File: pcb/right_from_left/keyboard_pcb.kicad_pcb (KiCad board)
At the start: 2 copper layers, 138.8 x 89.9 mm, 50 parts, among them J1 TRRS, K0 KEYSW, K1 KEYSW, K10 KEYSW, K11 KEYSW, K12 KEYSW, K13 KEYSW, K14 KEYSW, K15 KEYSW, K2 KEYSW, K20 KEYSW, K21 KEYSW, K22 KEYSW, K23 KEYSW, K24 KEYSW, K25 KEYSW, K3 KEYSW, K30 KEYSW, K31 KEYSW, K32 KEYSW, K4 KEYSW, K5 KEYSW, U1 MCP23009-E/SO, U2 Pico

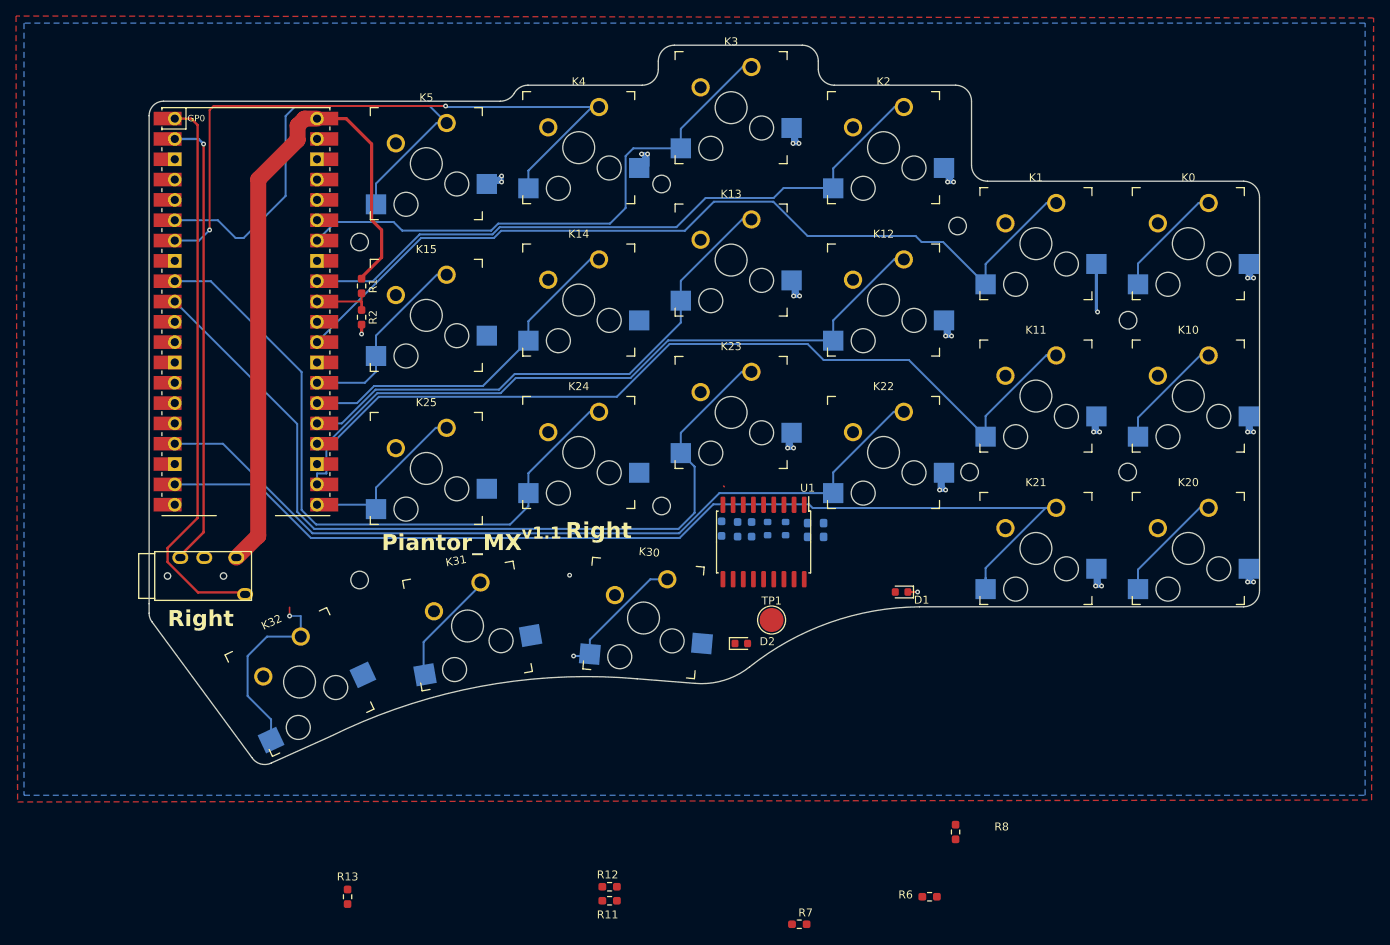
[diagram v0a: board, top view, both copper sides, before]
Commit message: Revision 1.1 -RFR- new standoff holes added and left/right pcb positions synced
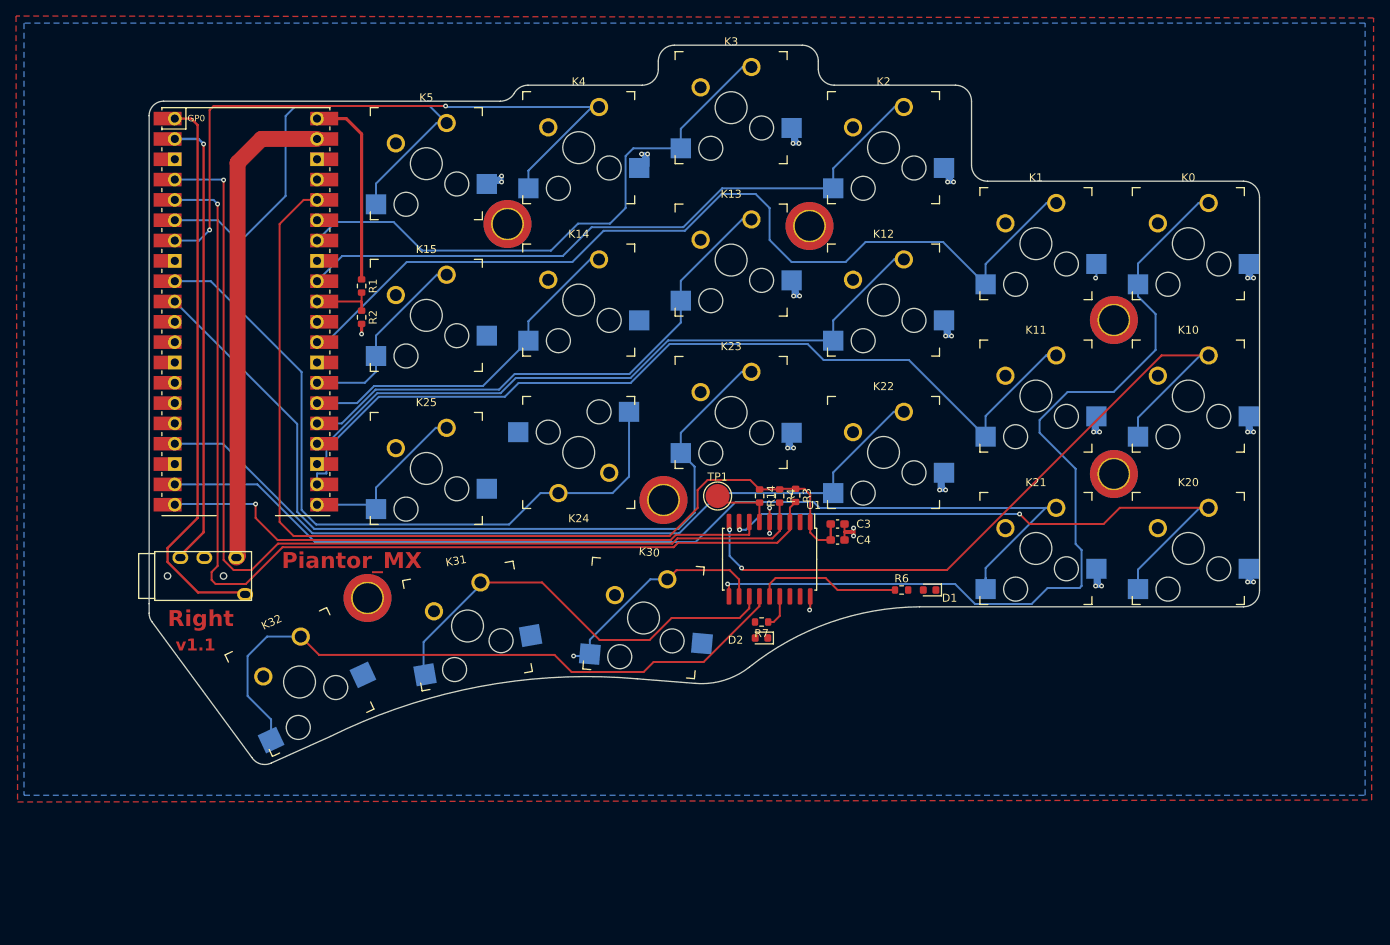
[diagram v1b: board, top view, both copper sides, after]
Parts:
- removed H7, H8: MountingHole, beekeeb_lib:MountingHole_2.2mm_M2-8mm
- removed R10, R11, R12, R13, R8, R9: 10k, Resistor_SMD:R_0603_1608Metric_Pad0.98x0.95mm_HandSolder
- C3, C4, R3, R4: moved to F.Cu
- H1, H2, H3, H4, H5, H6: footprint beekeeb_lib:MountingHole_2.2mm_M2-8mm -> misc:MountingHole_3.7mm_Pad_TopBottom
- R1, R2, R6, R7: footprint Resistor_SMD:R_0603_1608Metric_Pad0.98x0.95mm_HandSolder -> Resistor_SMD:R_0603_1608Metric
- R14: footprint Resistor_SMD:R_0603_1608Metric_Pad0.98x0.95mm_HandSolder -> Resistor_SMD:R_0603_1608Metric; moved to F.Cu
- moved R6 38.5 mm to (160.5, 111.5)
- moved R7 38.1 mm to (143.0, 115.5), turned to 180 degrees
- moved H5 22.8 mm to (187.0, 77.8)
- moved H1 19.2 mm to (149.0, 66.0)
- moved H2 18.6 mm to (111.2, 65.8)
- moved H6 18.0 mm to (187.0, 97.0)
- moved TP1 16.9 mm to (137.5, 99.8)
- moved R4 4.34 mm to (145.2, 99.8), turned to -90 degrees
- moved R3 4.33 mm to (147.2, 99.7), turned to -90 degrees
- moved R14 4.28 mm to (142.8, 99.8), turned to -90 degrees
- moved C4 3.95 mm to (152.5, 105.2), turned to 0 degrees
- moved D1 3.51 mm to (164.0, 111.5)
- moved D2 2.62 mm to (143.0, 117.5), turned to 180 degrees
- moved H3 2.46 mm to (93.7, 112.5)
- moved U1 2.28 mm to (144.0, 107.7)
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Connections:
- J1 pad 2: VBUS -> VCC
- U2 pad 39: unconnected-(U2-VSYS-Pad39) -> VCC
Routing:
- net /SCL: track 0.00 -> 132.0 mm, vias 0 -> 1
- net /SDA: track 0.00 -> 129.2 mm, vias 0 -> 1
- net +3.3V: track 0.00 -> 125.0 mm
- net /k00: track 14.6 -> 112.6 mm, vias 0 -> 1
- net /I2C_Int: track 0.00 -> 76.6 mm, vias 0 -> 1
- net /k10: track 14.4 -> 90.4 mm, vias 0 -> 2
- net VBUS: track 86.7 -> 24.5 mm
- net /k20: track 14.5 -> 76.3 mm, vias 0 -> 2
- net VCC: track 0.00 -> 60.6 mm
- net /k32: track 24.4 -> 83.2 mm, vias 1 -> 0
- net /k31: track 14.6 -> 54.3 mm, vias 1 -> 0
- net /LED_A: track 0.00 -> 18.2 mm
- net /k30: track 16.2 -> 28.3 mm
- net /MCP_RST: track 0.71 -> 8.03 mm
- net /k24: track 84.0 -> 90.1 mm
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
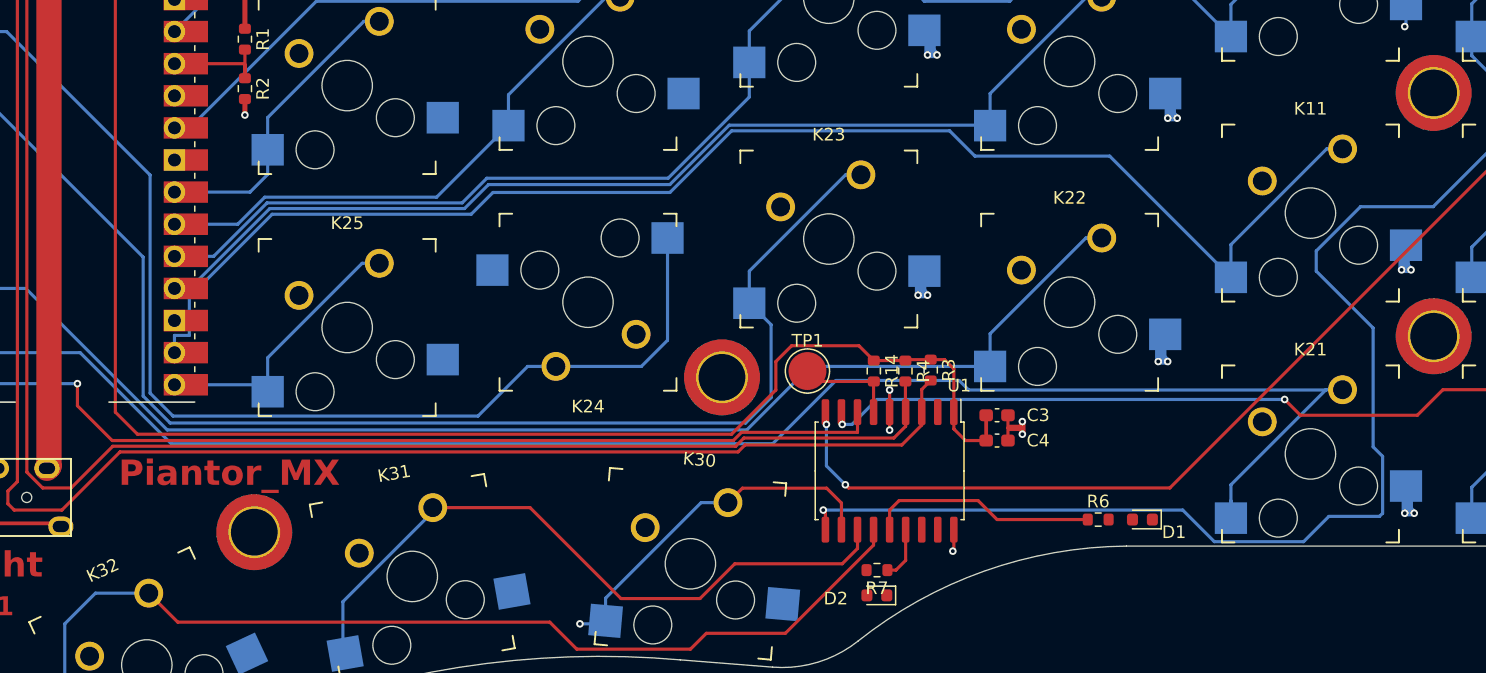
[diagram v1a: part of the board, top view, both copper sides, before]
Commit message: Revision 1.1 -RFR- right pcb layout fix
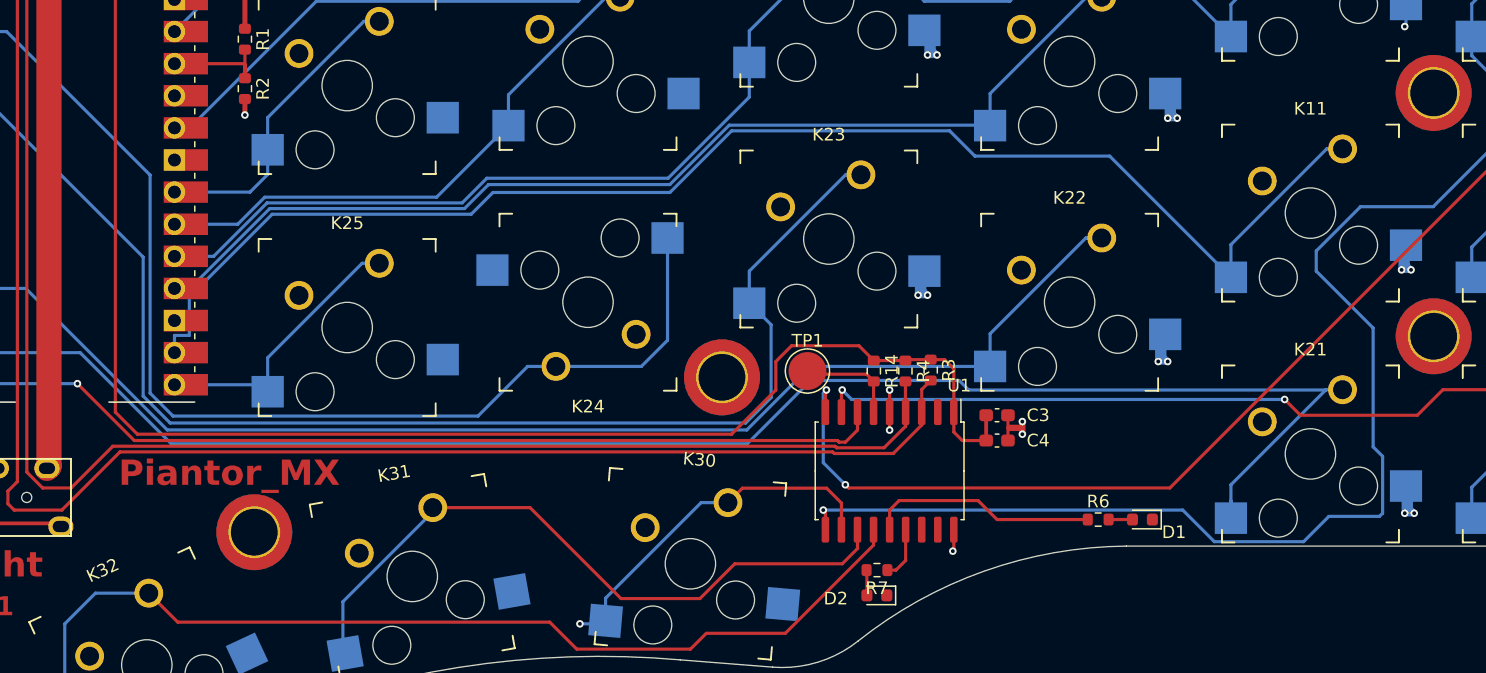
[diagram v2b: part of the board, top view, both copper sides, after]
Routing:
- net /k10: track 90.4 -> 94.1 mm
- net Net-(D2-A): track 0.00 -> 2.01 mm
- net Net-(D1-A): track 0.00 -> 1.89 mm
- net /I2C_Int: track 76.6 -> 75.6 mm
